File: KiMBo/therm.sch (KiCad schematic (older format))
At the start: 8 parts

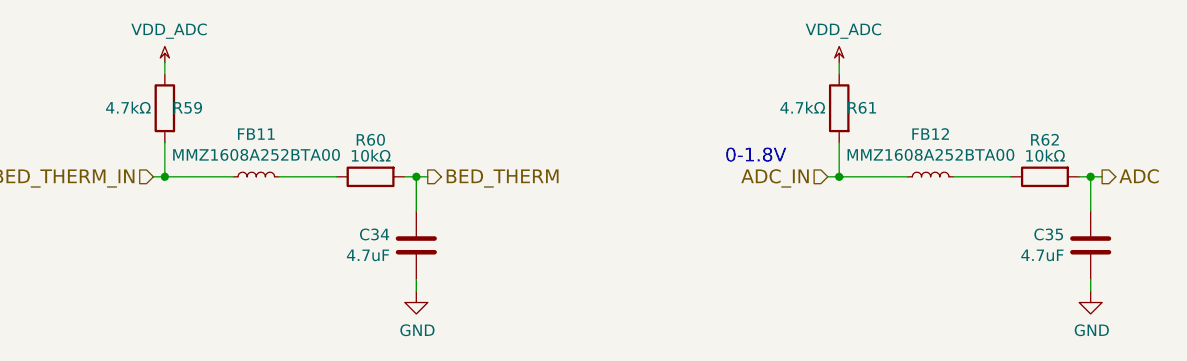
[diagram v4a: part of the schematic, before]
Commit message: Clean up various parts of the schematic, high level sheet has annoated modules
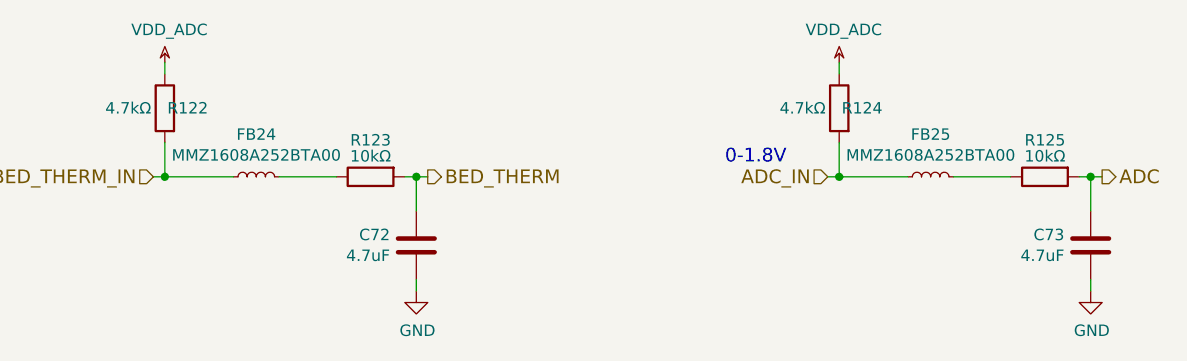
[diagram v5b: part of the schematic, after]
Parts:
- renumbered C34 to C72, C35 to C73, FB11 to FB24, FB12 to FB25, R59 to R122, R60 to R123, R61 to R124, R62 to R125
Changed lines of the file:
@@
 $Descr A3 16535 11693
 encoding utf-8
-Sheet 9 26
+Sheet 13 26
 Title ""
 Date ""
@@
 $EndDescr
 $Comp
-L C C34
+L C C72
 U 1 1 57931608
 P 6900 5550
-F 0 "C34" H 6785 5504 50  0000 R CNN
+F 0 "C72" H 6785 5504 50  0000 R CNN
 F 1 "4.7uF" H 6785 5595 50  0000 R CNN
 F 2 "" H 6938 5400 50  0000 C CNN
@@
 $EndComp
 $Comp
-L R R60
+L R R123
 U 1 1 57931779
 P 6700 5250
-F 0 "R60" V 6540 5250 50  0000 C CNN
+F 0 "R123" V 6540 5250 50  0000 C CNN
 F 1 "10kΩ" V 6610 5250 50  0000 C CNN
 F 2 "" V 6630 5250 50  0000 C CNN
@@
 $EndComp
 $Comp
-L R R59
+L R R122
 U 1 1 57931815
 P 5800 4950
-F 0 "R59" H 5700 4950 50  0000 C CNN
+F 0 "R122" H 5700 4950 50  0000 C CNN
 F 1 "4.7kΩ" H 5960 4950 50  0000 C CNN
 F 2 "" V 5730 4950 50  0000 C CNN
@@
 $EndComp
 $Comp
-L C C35
+L C C73
 U 1 1 5AD7EE6B
 P 9850 5550
-F 0 "C35" H 9735 5504 50  0000 R CNN
+F 0 "C73" H 9735 5504 50  0000 R CNN
 F 1 "4.7uF" H 9735 5595 50  0000 R CNN
 F 2 "" H 9888 5400 50  0000 C CNN
@@
 $EndComp
 $Comp
-L R R62
+L R R125
 U 1 1 5AD7EE80
 P 9650 5250
-F 0 "R62" V 9490 5250 50  0000 C CNN
+F 0 "R125" V 9490 5250 50  0000 C CNN
 F 1 "10kΩ" V 9560 5250 50  0000 C CNN
 F 2 "" V 9580 5250 50  0000 C CNN
@@
 $EndComp
 $Comp
-L R R61
+L R R124
 U 1 1 5AD7EE87
 P 8750 4950
-F 0 "R61" H 8650 4950 50  0000 C CNN
+F 0 "R124" H 8650 4950 50  0000 C CNN
 F 1 "4.7kΩ" H 8910 4950 50  0000 C CNN
 F 2 "" V 8680 4950 50  0000 C CNN
@@
 $EndComp
 $Comp
-L INDUCTOR_Small FB11
+L INDUCTOR_Small FB24
 U 1 1 5B885A27
 P 6200 5250
-F 0 "FB11" V 6385 5250 50  0000 C CNN
+F 0 "FB24" V 6385 5250 50  0000 C CNN
 F 1 "MMZ1608A252BTA00" V 6294 5250 50  0000 C CNN
 F 2 "" H 6200 5250 50  0000 C CNN
@@
 	8750 5250 8750 5100
 $Comp
-L INDUCTOR_Small FB12
+L INDUCTOR_Small FB25
 U 1 1 5B8FFD1D
 P 9150 5250
-F 0 "FB12" V 9335 5250 50  0000 C CNN
+F 0 "FB25" V 9335 5250 50  0000 C CNN
 F 1 "MMZ1608A252BTA00" V 9244 5250 50  0000 C CNN
 F 2 "" H 9150 5250 50  0000 C CNN

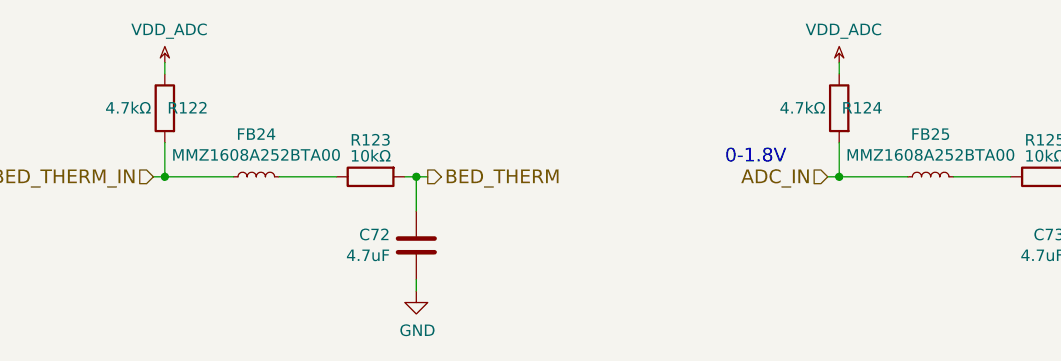
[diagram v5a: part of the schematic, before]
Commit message: Reorder the SS and EN lines from the shift registers such that the previously enabled/disabled motors stay enabled/disabled whilst writting to the shift register
Change 10k resistors to 4.7k, flip the open-drain inverter connected to B15 (PMTC_PGOOD)

Update the links in the README

Update the PDF schematic
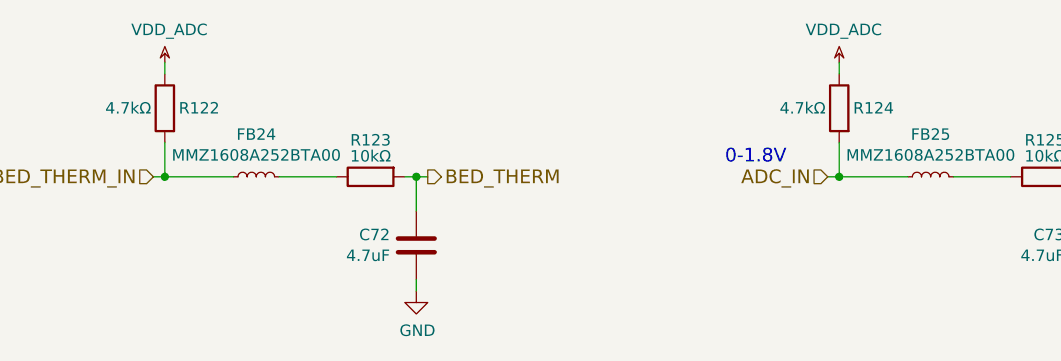
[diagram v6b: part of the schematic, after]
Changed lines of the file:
@@
 F 0 "C72" H 6785 5504 50  0000 R CNN
 F 1 "4.7uF" H 6785 5595 50  0000 R CNN
-F 2 "" H 6938 5400 50  0000 C CNN
+F 2 "" H 6938 5400 50  0001 C CNN
 F 3 "" H 6900 5550 50  0000 C CNN
 	1    6900 5550
@@
 F 0 "R123" V 6540 5250 50  0000 C CNN
 F 1 "10kΩ" V 6610 5250 50  0000 C CNN
-F 2 "" V 6630 5250 50  0000 C CNN
+F 2 "" V 6630 5250 50  0001 C CNN
 F 3 "" H 6700 5250 50  0000 C CNN
 	1    6700 5250
@@
 U 1 1 57931815
 P 5800 4950
-F 0 "R122" H 5700 4950 50  0000 C CNN
+F 0 "R122" H 5650 4950 50  0000 C CNN
 F 1 "4.7kΩ" H 5960 4950 50  0000 C CNN
-F 2 "" V 5730 4950 50  0000 C CNN
+F 2 "" V 5730 4950 50  0001 C CNN
 F 3 "" H 5800 4950 50  0000 C CNN
 	1    5800 4950
@@
 F 0 "C73" H 9735 5504 50  0000 R CNN
 F 1 "4.7uF" H 9735 5595 50  0000 R CNN
-F 2 "" H 9888 5400 50  0000 C CNN
+F 2 "" H 9888 5400 50  0001 C CNN
 F 3 "" H 9850 5550 50  0000 C CNN
 	1    9850 5550
@@
 F 0 "R125" V 9490 5250 50  0000 C CNN
 F 1 "10kΩ" V 9560 5250 50  0000 C CNN
-F 2 "" V 9580 5250 50  0000 C CNN
+F 2 "" V 9580 5250 50  0001 C CNN
 F 3 "" H 9650 5250 50  0000 C CNN
 	1    9650 5250
@@
 U 1 1 5AD7EE87
 P 8750 4950
-F 0 "R124" H 8650 4950 50  0000 C CNN
+F 0 "R124" H 8600 4950 50  0000 C CNN
 F 1 "4.7kΩ" H 8910 4950 50  0000 C CNN
-F 2 "" V 8680 4950 50  0000 C CNN
+F 2 "" V 8680 4950 50  0001 C CNN
 F 3 "" H 8750 4950 50  0000 C CNN
 	1    8750 4950
@@
 F 0 "FB24" V 6385 5250 50  0000 C CNN
 F 1 "MMZ1608A252BTA00" V 6294 5250 50  0000 C CNN
-F 2 "" H 6200 5250 50  0000 C CNN
+F 2 "" H 6200 5250 50  0001 C CNN
 F 3 "" H 6200 5250 50  0000 C CNN
 	1    6200 5250
@@
 F 0 "FB25" V 9335 5250 50  0000 C CNN
 F 1 "MMZ1608A252BTA00" V 9244 5250 50  0000 C CNN
-F 2 "" H 9150 5250 50  0000 C CNN
+F 2 "" H 9150 5250 50  0001 C CNN
 F 3 "" H 9150 5250 50  0000 C CNN
 	1    9150 5250

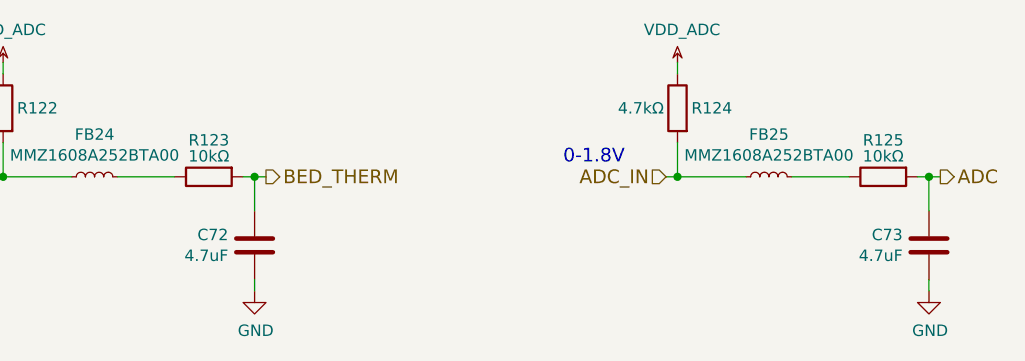
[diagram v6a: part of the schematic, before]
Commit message: Begin entry of component values
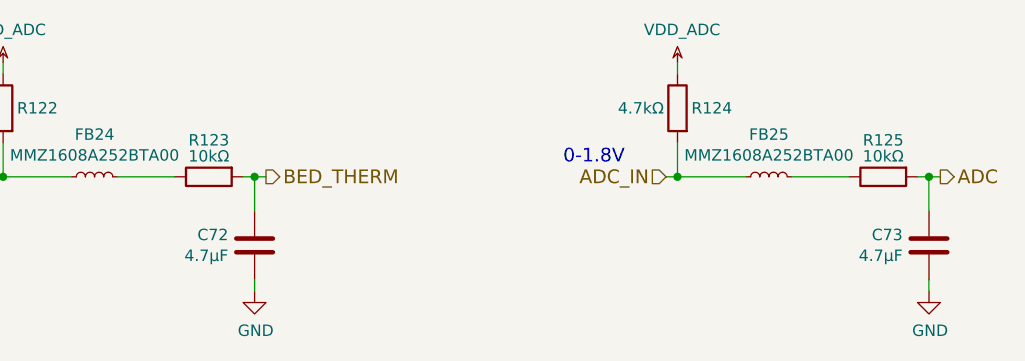
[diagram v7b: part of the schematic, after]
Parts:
- C72, C73: value 4.7uF -> 4.7μF
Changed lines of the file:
@@
 P 6900 5550
 F 0 "C72" H 6785 5504 50  0000 R CNN
-F 1 "4.7uF" H 6785 5595 50  0000 R CNN
+F 1 "4.7μF" H 6785 5595 50  0000 R CNN
 F 2 "" H 6938 5400 50  0001 C CNN
 F 3 "" H 6900 5550 50  0000 C CNN
@@
 P 9850 5550
 F 0 "C73" H 9735 5504 50  0000 R CNN
-F 1 "4.7uF" H 9735 5595 50  0000 R CNN
+F 1 "4.7μF" H 9735 5595 50  0000 R CNN
 F 2 "" H 9888 5400 50  0001 C CNN
 F 3 "" H 9850 5550 50  0000 C CNN

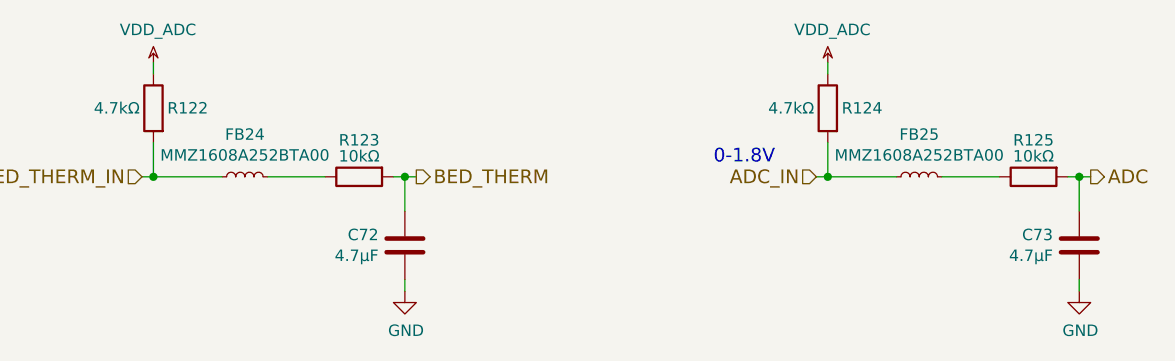
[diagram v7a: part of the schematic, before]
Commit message: Entry of additional component values
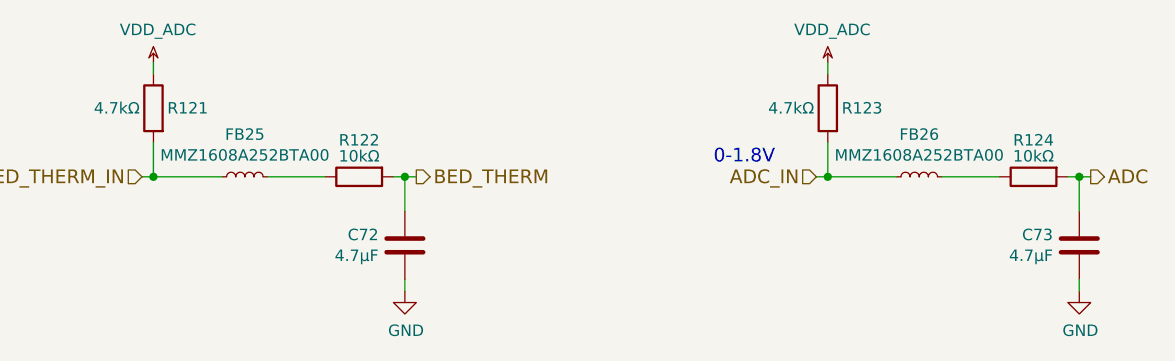
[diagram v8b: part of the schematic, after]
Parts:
- renumbered FB24 to FB25, FB25 to FB26, R122 to R121, R123 to R122, R124 to R123, R125 to R124
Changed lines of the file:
@@
 $EndComp
 $Comp
-L R R123
+L R R122
 U 1 1 57931779
 P 6700 5250
-F 0 "R123" V 6540 5250 50  0000 C CNN
+F 0 "R122" V 6540 5250 50  0000 C CNN
 F 1 "10kΩ" V 6610 5250 50  0000 C CNN
 F 2 "" V 6630 5250 50  0001 C CNN
@@
 $EndComp
 $Comp
-L R R122
+L R R121
 U 1 1 57931815
 P 5800 4950
-F 0 "R122" H 5650 4950 50  0000 C CNN
+F 0 "R121" H 5650 4950 50  0000 C CNN
 F 1 "4.7kΩ" H 5960 4950 50  0000 C CNN
 F 2 "" V 5730 4950 50  0001 C CNN
@@
 BED_THERM_IN
 $Comp
-L VDD_ADC #PWR0175
+L VDD_ADC #PWR0176
 U 1 1 59E74D42
 P 5800 4750
-F 0 "#PWR0175" H 5950 4700 50  0001 C CNN
+F 0 "#PWR0176" H 5950 4700 50  0001 C CNN
 F 1 "VDD_ADC" H 5820 4893 50  0000 C CNN
 F 2 "" H 5800 4750 50  0000 C CNN
@@
 $EndComp
 $Comp
-L R R125
+L R R124
 U 1 1 5AD7EE80
 P 9650 5250
-F 0 "R125" V 9490 5250 50  0000 C CNN
+F 0 "R124" V 9490 5250 50  0000 C CNN
 F 1 "10kΩ" V 9560 5250 50  0000 C CNN
 F 2 "" V 9580 5250 50  0001 C CNN
@@
 $EndComp
 $Comp
-L R R124
+L R R123
 U 1 1 5AD7EE87
 P 8750 4950
-F 0 "R124" H 8600 4950 50  0000 C CNN
+F 0 "R123" H 8600 4950 50  0000 C CNN
 F 1 "4.7kΩ" H 8910 4950 50  0000 C CNN
 F 2 "" V 8680 4950 50  0001 C CNN
@@
 ADC_IN
 $Comp
-L VDD_ADC #PWR0176
+L VDD_ADC #PWR0177
 U 1 1 5AD7EEB1
 P 8750 4750
-F 0 "#PWR0176" H 8900 4700 50  0001 C CNN
+F 0 "#PWR0177" H 8900 4700 50  0001 C CNN
 F 1 "VDD_ADC" H 8770 4893 50  0000 C CNN
 F 2 "" H 8750 4750 50  0000 C CNN
@@
 $EndComp
 $Comp
-L GND #PWR0177
+L GND #PWR0178
 U 1 1 5B331170
 P 6900 5750
-F 0 "#PWR0177" H 6900 5500 50  0001 C CNN
+F 0 "#PWR0178" H 6900 5500 50  0001 C CNN
 F 1 "GND" H 6905 5577 50  0000 C CNN
 F 2 "" H 6900 5750 50  0000 C CNN
@@
 $EndComp
 $Comp
-L GND #PWR0178
+L GND #PWR0179
 U 1 1 5B3311A0
 P 9850 5750
-F 0 "#PWR0178" H 9850 5500 50  0001 C CNN
+F 0 "#PWR0179" H 9850 5500 50  0001 C CNN
 F 1 "GND" H 9855 5577 50  0000 C CNN
 F 2 "" H 9850 5750 50  0000 C CNN
@@
 $EndComp
 $Comp
-L INDUCTOR_Small FB24
+L INDUCTOR_Small FB25
 U 1 1 5B885A27
 P 6200 5250
-F 0 "FB24" V 6385 5250 50  0000 C CNN
+F 0 "FB25" V 6385 5250 50  0000 C CNN
 F 1 "MMZ1608A252BTA00" V 6294 5250 50  0000 C CNN
 F 2 "" H 6200 5250 50  0001 C CNN
@@
 	8750 5250 8750 5100
 $Comp
-L INDUCTOR_Small FB25
+L INDUCTOR_Small FB26
 U 1 1 5B8FFD1D
 P 9150 5250
-F 0 "FB25" V 9335 5250 50  0000 C CNN
+F 0 "FB26" V 9335 5250 50  0000 C CNN
 F 1 "MMZ1608A252BTA00" V 9244 5250 50  0000 C CNN
 F 2 "" H 9150 5250 50  0001 C CNN
